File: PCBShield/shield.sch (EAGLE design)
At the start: 69 parts

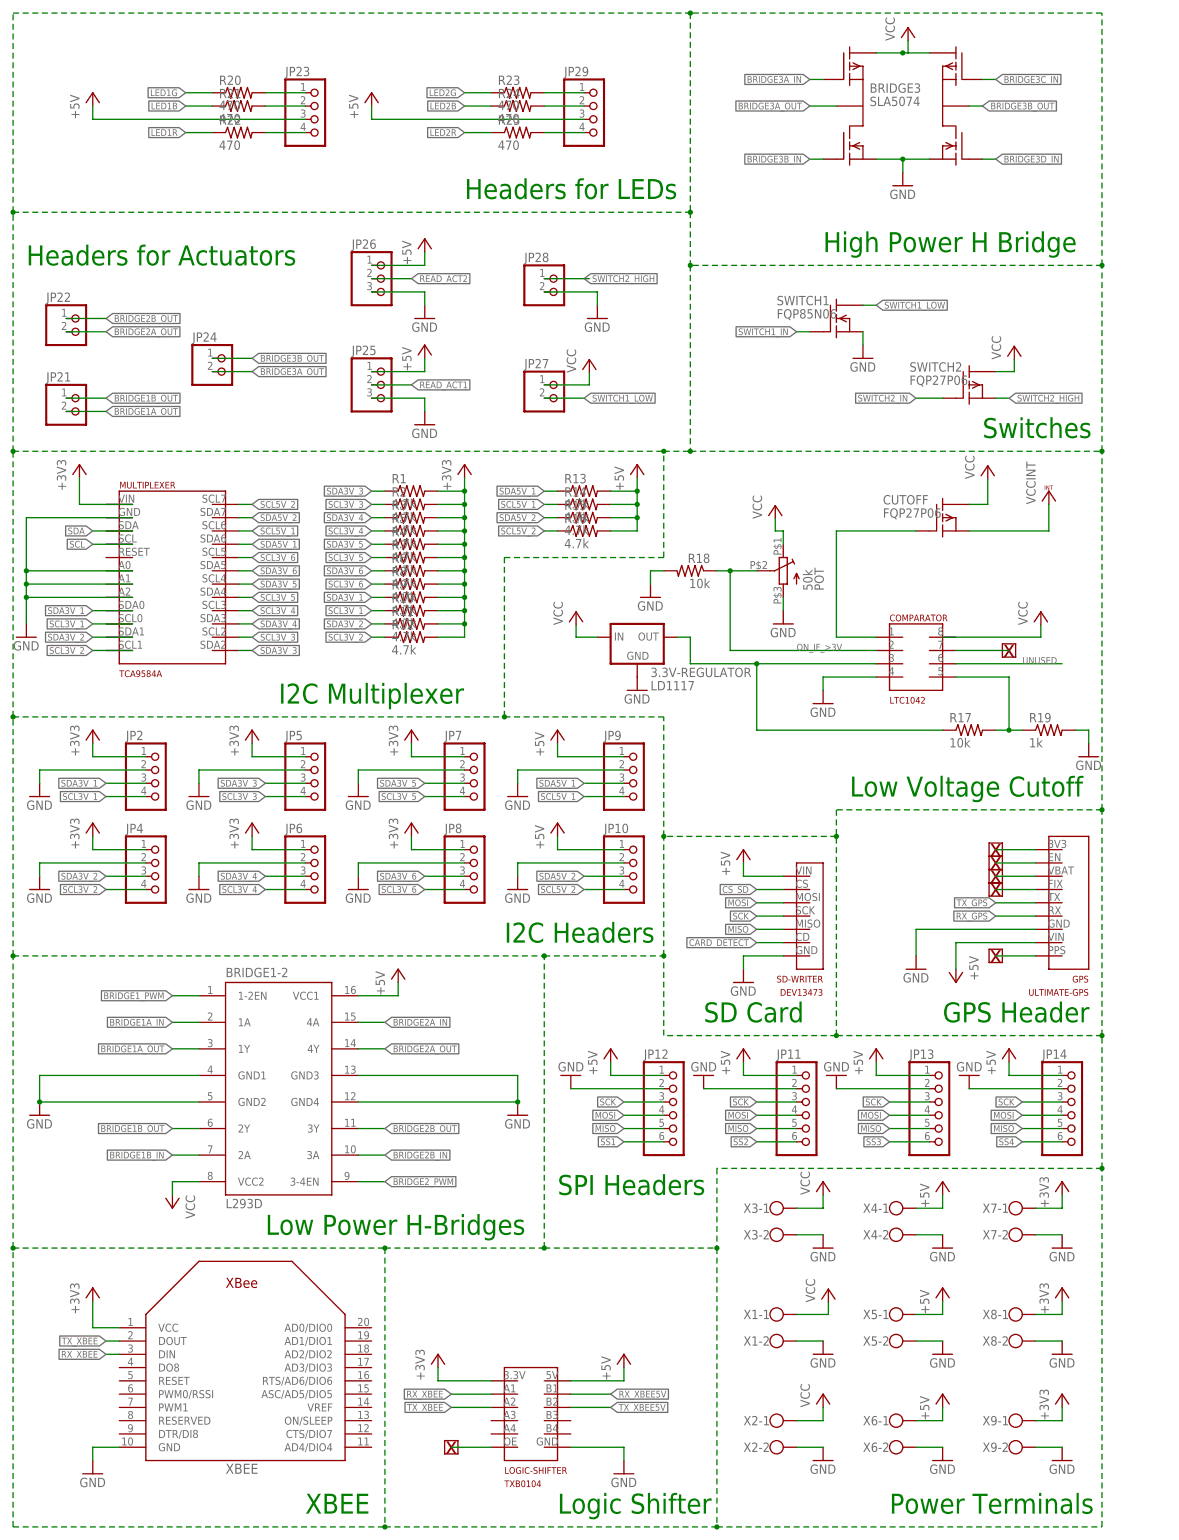
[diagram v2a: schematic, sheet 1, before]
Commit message: Preliminary arrangement of components on board complete, and several connections on schematic have been fixed.
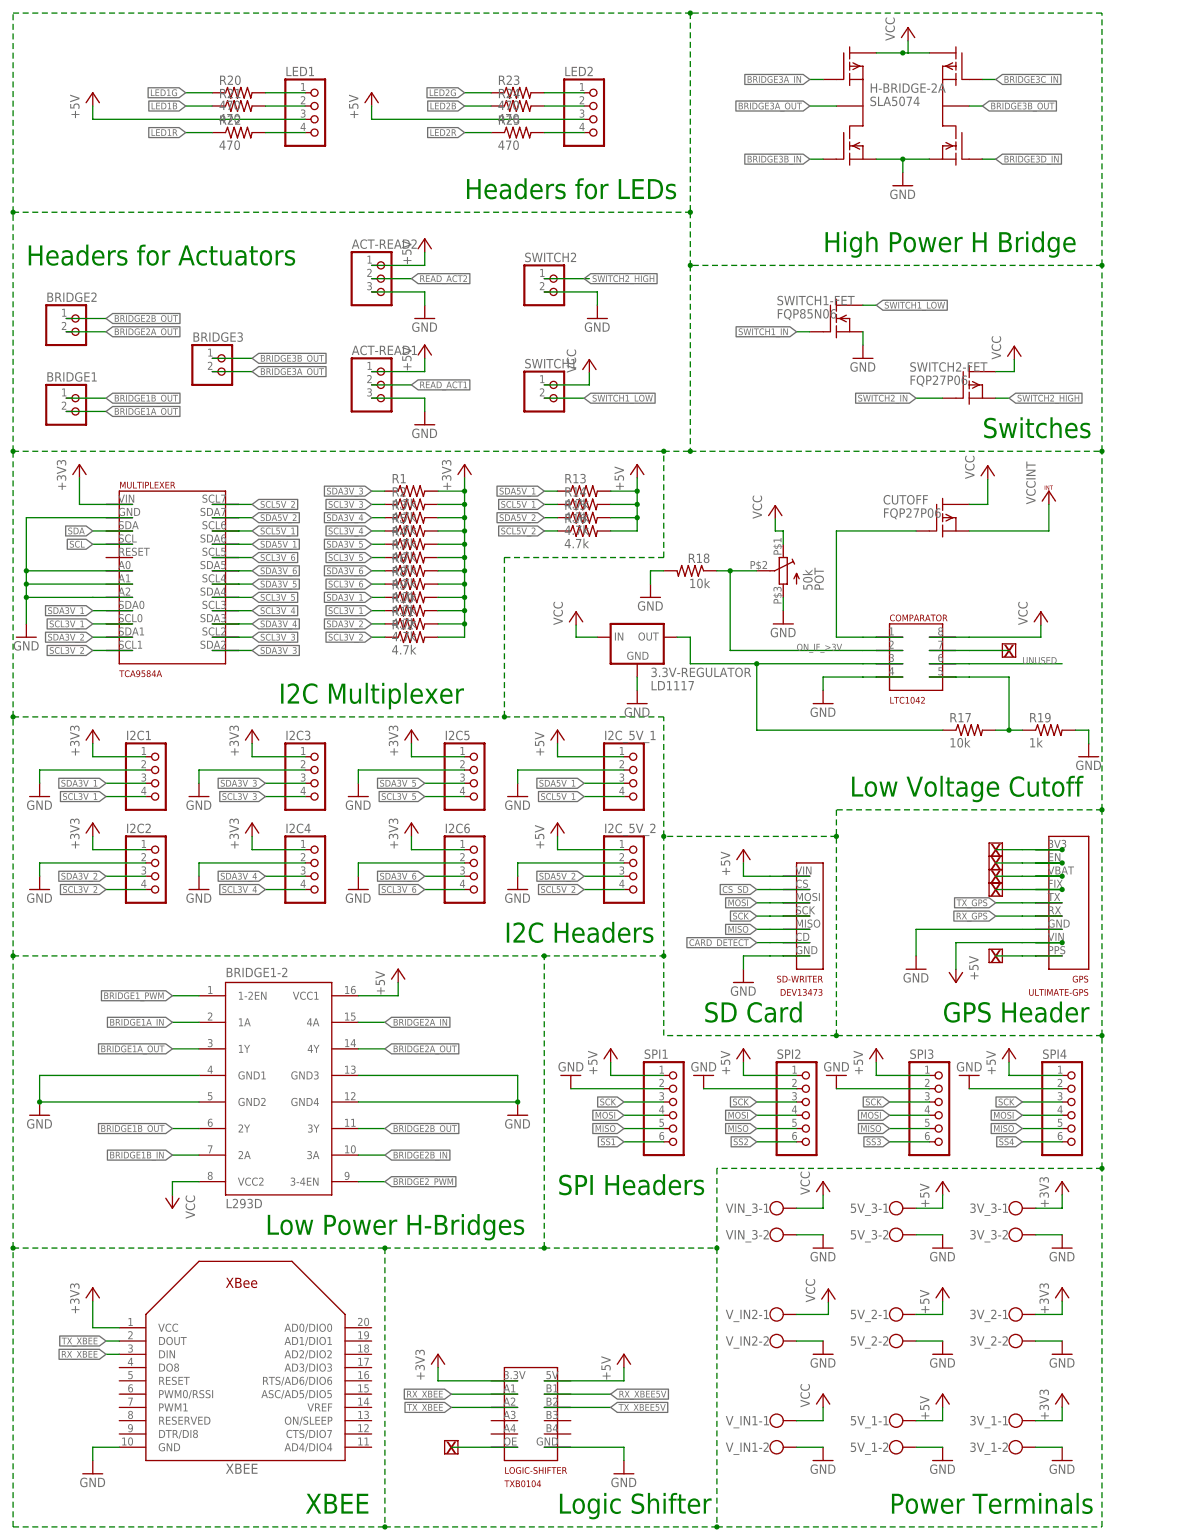
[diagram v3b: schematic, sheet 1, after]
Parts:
- removed JP24, JP27, JP28: (no value), pinhead:PINHD-1X2
- added H-BRIDGE-2A: SLA5074, specialparts:SLA5074
- added SWITCH1-FET: FQP85N06, specialparts:FQP85N06
- added SWITCH2-FET: FQP27P06, specialparts:FQP27P06
- BRIDGE3: value SLA5074 -> (none); device specialparts:SLA5074 -> pinhead:PINHD-1X2
- SWITCH1: value FQP85N06 -> (none); device specialparts:FQP85N06 -> pinhead:PINHD-1X2
- SWITCH2: value FQP27P06 -> (none); device specialparts:FQP27P06 -> pinhead:PINHD-1X2
- renumbered JP10 to I2C_5V_2, JP11 to SPI2, JP12 to SPI1, JP13 to SPI3, JP14 to SPI4, JP2 to I2C1, JP21 to BRIDGE1, JP22 to BRIDGE2, JP23 to LED1, JP25 to ACT-READ1, JP26 to ACT-READ2, JP29 to LED2, JP4 to I2C2, JP5 to I2C3, JP6 to I2C4, JP7 to I2C5, JP8 to I2C6, JP9 to I2C_5V_1, X1 to V_IN2, X2 to V_IN1, X3 to VIN_3, X4 to 5V_3, X5 to 5V_2, X6 to 5V_1, X7 to 3V_3, X8 to 3V_2, X9 to 3V_1
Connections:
- removed net N$19: 3.3V-REGULATOR.VOUT, R17.1
- new net CARD_DETECT: SD-WRITER.CD
- new net N$10: GPS.EN
- new net N$11: GPS.VBAT
- new net N$12: GPS.FIX
- new net N$13: LOGIC-SHIFTER.OE
- new net N$15: COMPARATOR.OSC
- new net N$17: GPS.PPS
- new net N$9: GPS.3V3
- new net REG-3V3: 3.3V-REGULATOR.VOUT, COMPARATOR.VIN, R17.1
- new net UNUSED: COMPARATOR.ABOVE-WINDOW
- net +3V3: now also LOGIC-SHIFTER.3V3
- net +5V: now also GPS.VIN, LOGIC-SHIFTER.5V, SD-WRITER.VIN
- net BRIDGE3A_IN: now also H-BRIDGE-2A.P$4; no longer BRIDGE3.P$4
- net BRIDGE3A_OUT: now also BRIDGE3.2, H-BRIDGE-2A.P$3; no longer BRIDGE3.P$3, JP24.2
- net BRIDGE3B_IN: now also H-BRIDGE-2A.P$2; no longer BRIDGE3.P$2
- net BRIDGE3B_OUT: now also BRIDGE3.1, H-BRIDGE-2A.P$7; no longer BRIDGE3.P$7, JP24.1
- net BRIDGE3C_IN: now also H-BRIDGE-2A.P$9; no longer BRIDGE3.P$9
- net BRIDGE3D_IN: now also H-BRIDGE-2A.P$6; no longer BRIDGE3.P$6
- net CS_SD: now also SD-WRITER.CS
- net GND: now also 3.3V-REGULATOR.GND, COMPARATOR.GND, GPS.GND, H-BRIDGE-2A.P$1, H-BRIDGE-2A.P$8, LOGIC-SHIFTER.GND, SD-WRITER.GND, SWITCH1-FET.S, SWITCH2.2; no longer BRIDGE3.P$1, BRIDGE3.P$8, JP28.2, SWITCH1.S
- net MISO: now also SD-WRITER.MISO
- net MOSI: now also SD-WRITER.MOSI
- net N$16: now also COMPARATOR.WIDTH/2
- net N$18: now also COMPARATOR.WITHIN-WINDOW
- net ON_IF_>3V: now also COMPARATOR.CENTER
- net RX_GPS: now also GPS.RX
- net RX_XBEE: now also LOGIC-SHIFTER.A1
- net RX_XBEE5V: now also LOGIC-SHIFTER.B1
- net SCK: now also SD-WRITER.SCK
- net SCL3V_3: now also MULTIPLEXER.SCL2
- net SCL3V_4: now also MULTIPLEXER.SCL3
- net SCL3V_5: now also MULTIPLEXER.SDA4
- net SCL3V_6: now also MULTIPLEXER.SCL5
- net SCL5V_1: now also MULTIPLEXER.SCL6
- net SCL5V_2: now also MULTIPLEXER.SCL7
- net SDA3V_3: now also MULTIPLEXER.SDA2
- net SDA3V_4: now also MULTIPLEXER.SDA3
- net SDA3V_5: now also MULTIPLEXER.SCL4
- net SDA3V_6: now also MULTIPLEXER.SDA5
- net SDA5V_1: now also MULTIPLEXER.SDA6
- net SDA5V_2: now also MULTIPLEXER.SDA7
- net SWITCH1_LOW: now also SWITCH1.2; no longer JP27.2
- net SWITCH2_HIGH: now also SWITCH2-FET.S, SWITCH2.1; no longer JP28.1, SWITCH2.S
- net SWITCH2_IN: now also SWITCH2-FET.G; no longer SWITCH2.G
- net TX_GPS: now also GPS.TX
- net TX_XBEE: now also LOGIC-SHIFTER.A2
- net TX_XBEE5V: now also LOGIC-SHIFTER.B2
- net VCC: now also COMPARATOR.V+, H-BRIDGE-2A.P$10, H-BRIDGE-2A.P$5, SWITCH1.1, SWITCH2-FET.D; no longer BRIDGE3.P$10, BRIDGE3.P$5, JP27.1, SWITCH2.D

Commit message: Board is laid out and ready for routing. Screw terminals replace
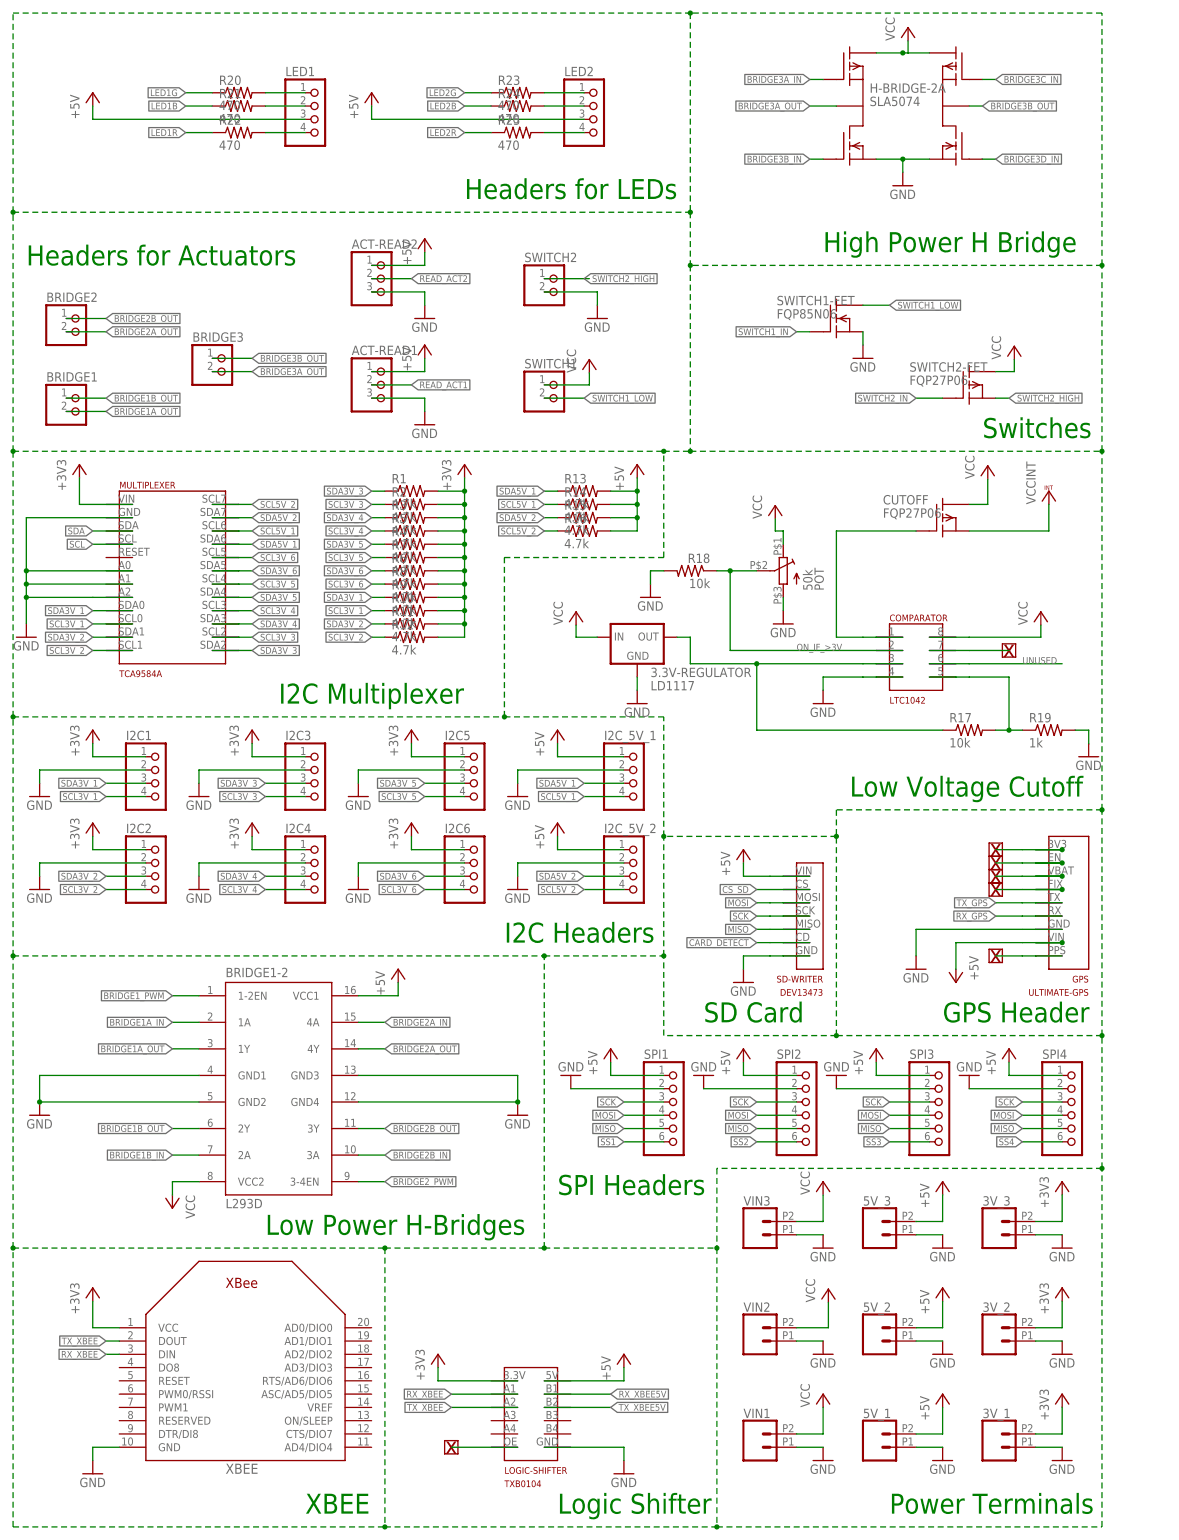
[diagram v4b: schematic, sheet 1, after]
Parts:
- removed VIN_3, V_IN1, V_IN2: (no value), con-wago-500:W237-102
- added VIN1, VIN2, VIN3: (no value), SparkFun-Connectors:CONN_022.54MM_SCREWTERM
- 3V_1, 3V_2, 3V_3, 5V_1, 5V_2, 5V_3: device con-wago-500:W237-102 -> SparkFun-Connectors:CONN_022.54MM_SCREWTERM
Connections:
- net N$18 renamed POWER-ON
- net +3V3: no longer 3V_1-1.KL, 3V_2-1.KL, 3V_3-1.KL
- net +5V: no longer 5V_1-1.KL, 5V_2-1.KL, 5V_3-1.KL
- net GND: now also 3V_1.1, 3V_2.1, 3V_3.1, 5V_1.1, 5V_2.1, 5V_3.1, PCB2.GND..., VIN1.1, VIN2.1, VIN3.1; no longer 3V_1-2.KL, 3V_2-2.KL, 3V_3-2.KL, 5V_1-2.KL, 5V_2-2.KL, 5V_3-2.KL, VIN_3-2.KL, V_IN1-2.KL, V_IN2-2.KL
- net SCL3V_5: now also MULTIPLEXER.SCL4; no longer MULTIPLEXER.SDA4
- net SDA3V_5: now also MULTIPLEXER.SDA4; no longer MULTIPLEXER.SCL4
- net SWITCH1_IN: now also SWITCH1-FET.G
- net SWITCH1_LOW: now also SWITCH1-FET.D
- net VCC: no longer VIN_3-1.KL, V_IN1-1.KL, V_IN2-1.KL

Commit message: First version of board complete including routing, pending verification
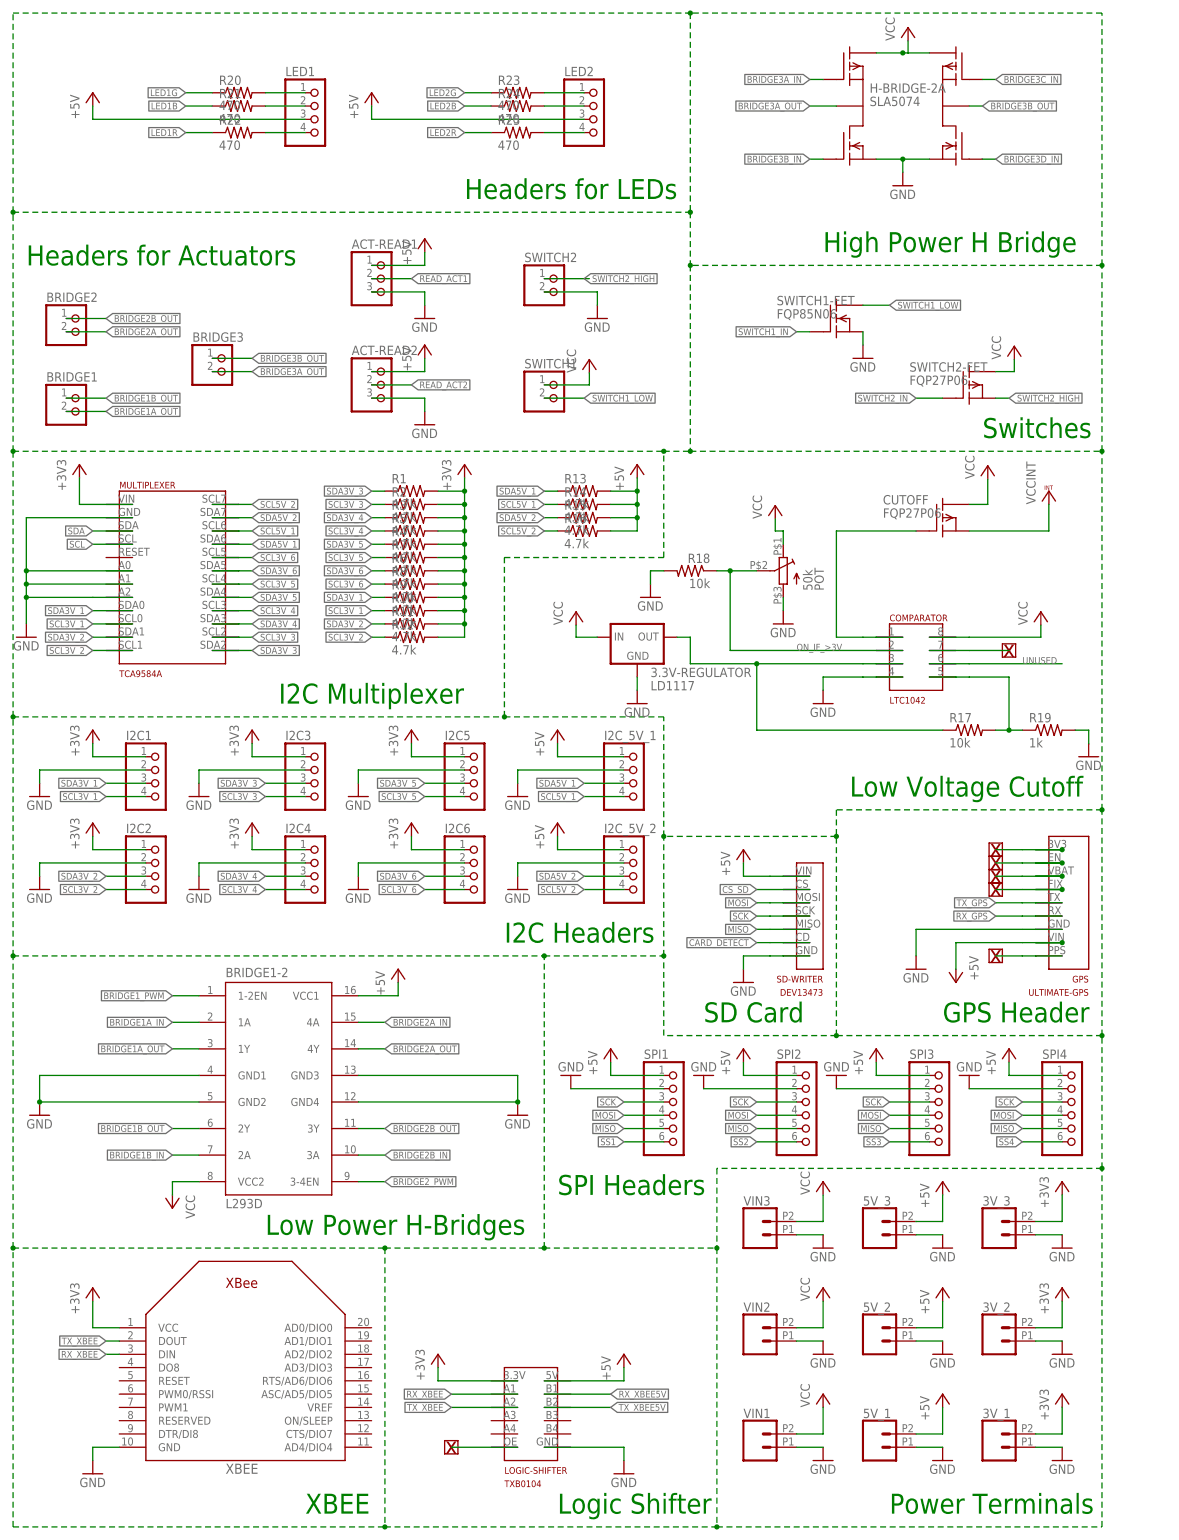
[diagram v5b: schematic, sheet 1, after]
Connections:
- net N$16 renamed 0.3V
- net +3V3: now also 3V_1.2, 3V_2.2, 3V_3.2
- net +5V: now also 5V_1.2, 5V_2.2, 5V_3.2, PCB2.+5V., PCB2.+5V..
- net GND: now also PCB2.GND....
- net LED1B: now also PCB2.33; no longer PCB2.36
- net LED1G: now also PCB2.35; no longer PCB2.34
- net LED2G: now also PCB2.36; no longer PCB2.35
- net LED2R: now also PCB2.34; no longer PCB2.33
- net VCC: now also VIN1.2, VIN2.2, VIN3.2
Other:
- moved on the sheet: ACT-READ1, ACT-READ2

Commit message: Final version of PCB for printing
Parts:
- added U$1: 6BOLT, specialparts:6BOLT
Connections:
- net GND: now also U$1.P$1
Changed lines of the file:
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@@
 <part name="3V_3" library="SparkFun-Connectors" library_urn="urn:adsk.eagle:library:513" deviceset="CONN_02" device="2.54MM_SCREWTERM" package3d_urn="urn:adsk.eagle:package:38059/1"/>
 <part name="P+28" library="supply1" library_urn="urn:adsk.eagle:library:371" deviceset="+5V" device=""/>
+<part name="U$1" library="specialparts" deviceset="6BOLT" device=""/>
+<part name="GND42" library="supply1" library_urn="urn:adsk.eagle:library:371" deviceset="GND" device=""/>
 </parts>
 <sheets>
@@
 <instance part="3V_2" gate="G$1" x="187.96" y="35.56"/>
 <instance part="3V_3" gate="G$1" x="187.96" y="55.88"/>
+<instance part="U$1" gate="G$1" x="132.08" y="139.7"/>
+<instance part="GND42" gate="1" x="147.32" y="137.16"/>
 </instances>
 <busses>
@@
 <wire x1="119.38" y1="160.02" x2="119.38" y2="162.56" width="0.1524" layer="91"/>
 </segment>
+<segment>
+<pinref part="U$1" gate="G$1" pin="P$1"/>
+<pinref part="GND42" gate="1" pin="GND"/>
+<wire x1="132.08" y1="139.7" x2="147.32" y2="139.7" width="0.1524" layer="91"/>
+</segment>
 </net>
